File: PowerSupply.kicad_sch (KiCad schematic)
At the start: 44 parts, among them J1 Barrel_Jack, J2 PowerHeader, M1 MouseBites, M2 MouseBites, M3 MouseBites, M4 MouseBites, SW1 SW_SPST, U1 LM7805_TO220, U2 LM7812_TO220, U3 LM7912_TO220

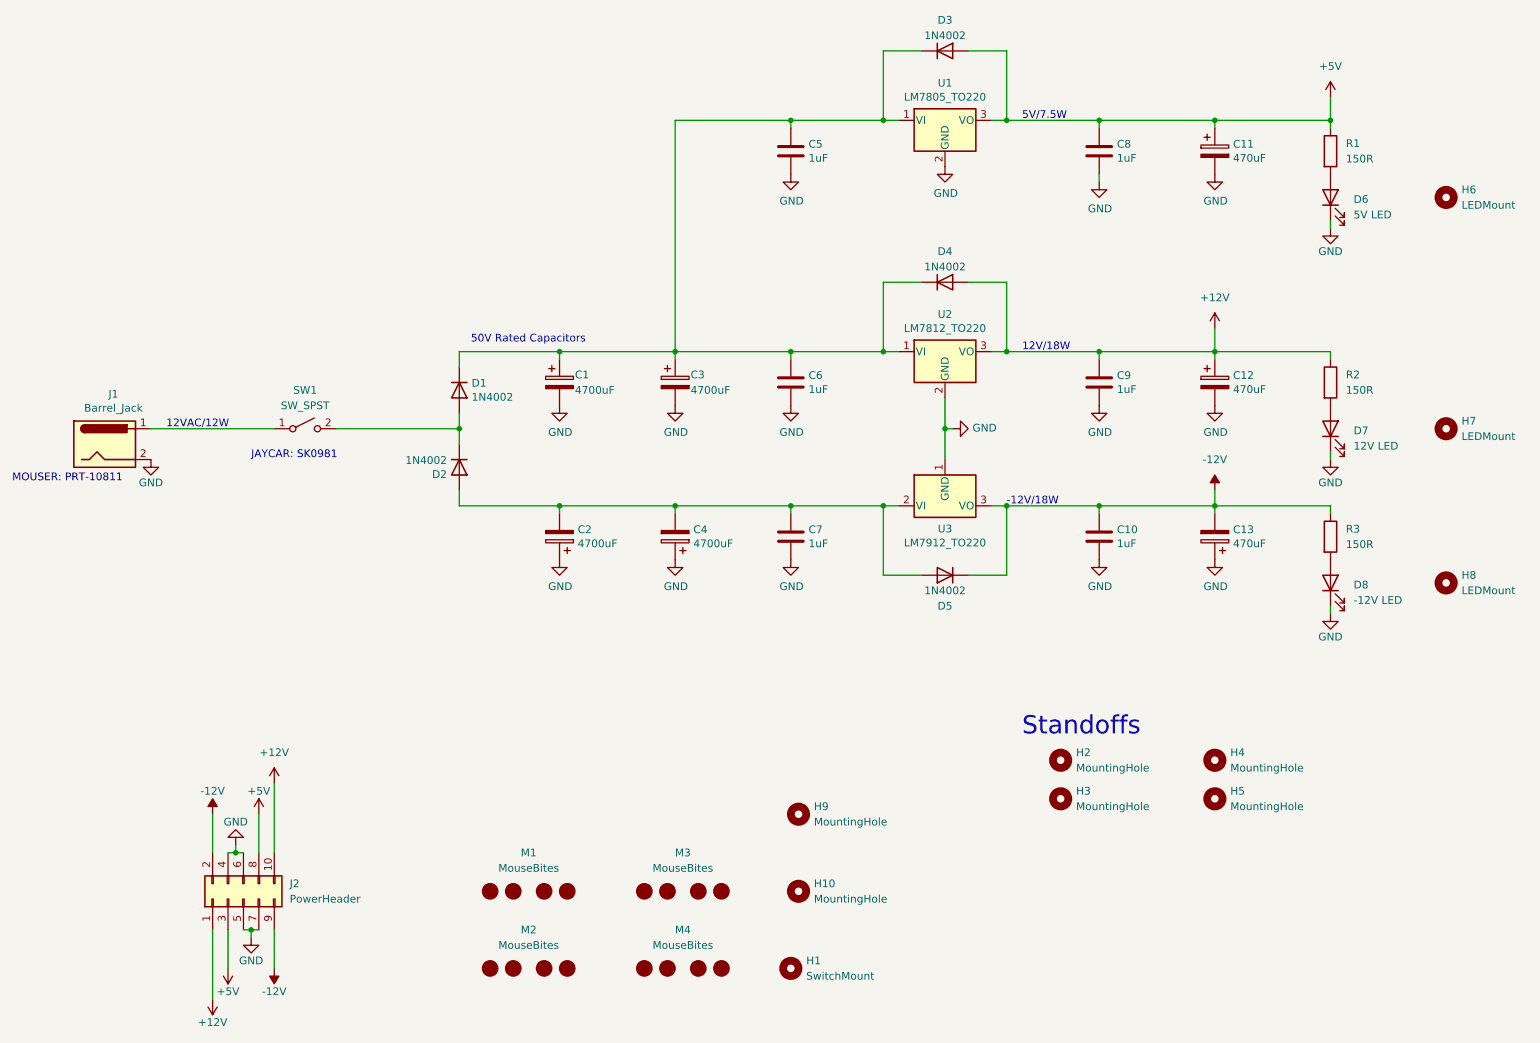
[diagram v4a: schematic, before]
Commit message: Preliminary design on rework
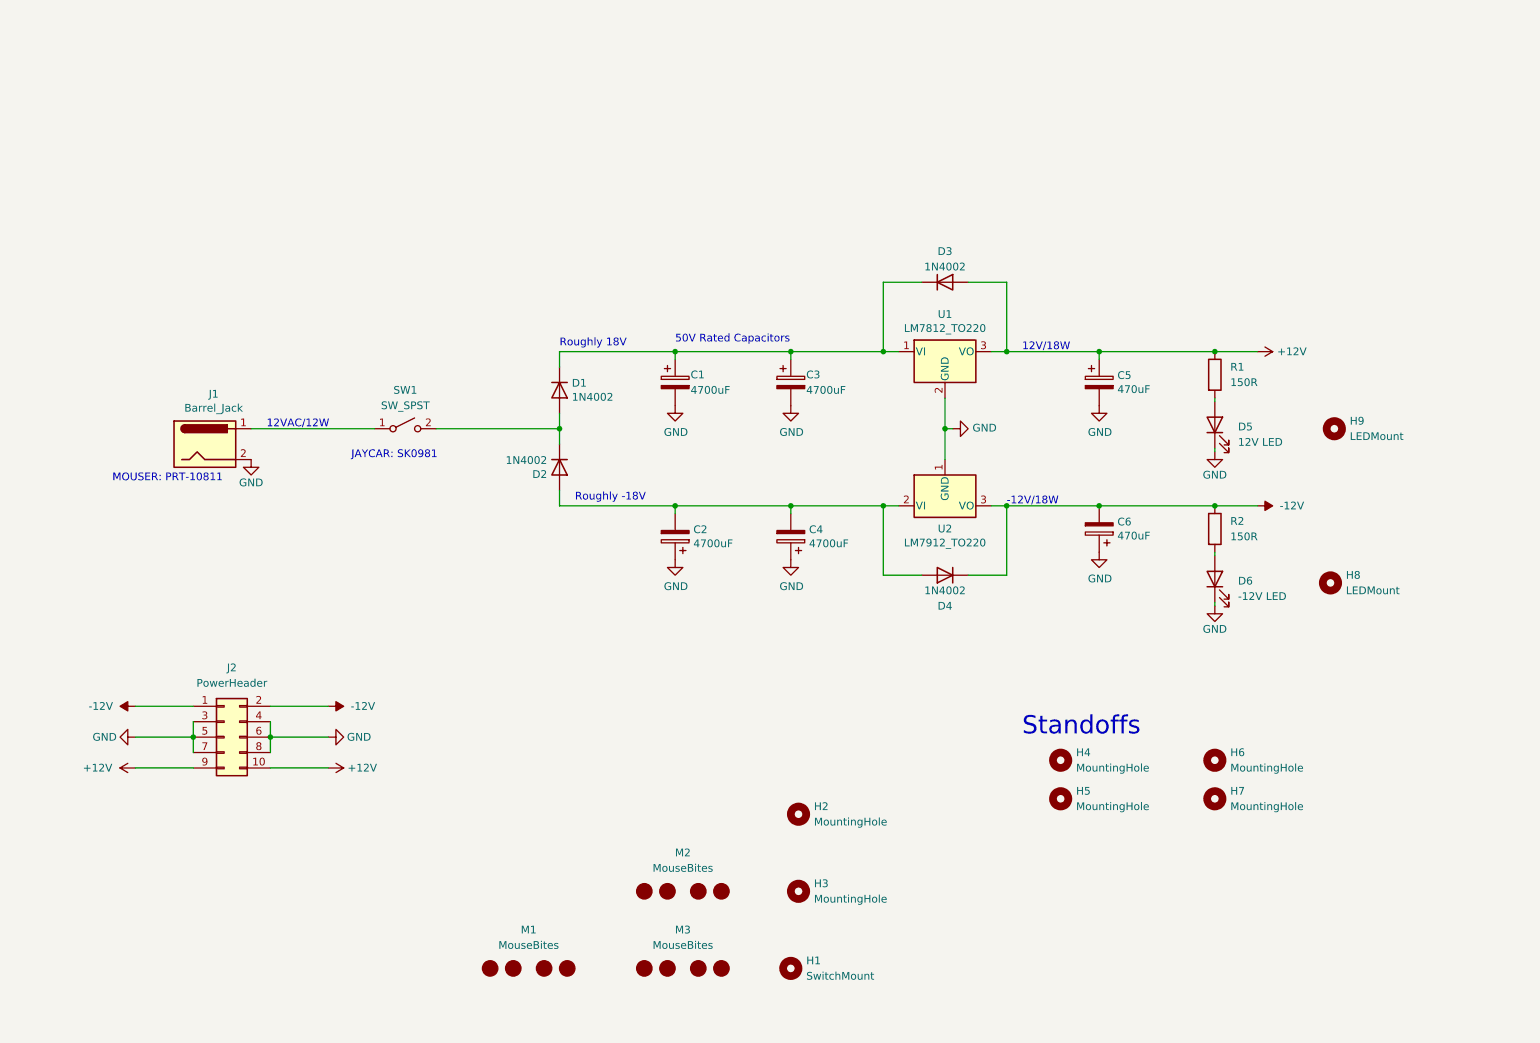
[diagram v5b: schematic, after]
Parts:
- removed C10, C5, C6, C7, C8, C9: 1uF, Capacitor_SMD:C_0805_2012Metric_Pad1.18x1.45mm_HandSolder, symbol Device:C
- removed C11: 470uF, Capacitor_THT:CP_Radial_D10.0mm_P5.00mm, symbol Device:CP
- removed D3: 1N4002, Diode_THT:D_DO-15_P12.70mm_Horizontal, symbol Device:D
- removed D6: 5V LED, LED_THT:LED_D5.0mm, symbol Device:LED
- removed H6: LEDMount, MountingHole:MountingHole_5mm, symbol Mechanical:MountingHole
- removed M1: MouseBites, Panelization:mouse-bite-5mm-slot, symbol Synth:MouseBites
- removed R1: 150R, Resistor_SMD:R_0805_2012Metric_Pad1.20x1.40mm_HandSolder, symbol Device:R
- removed U1: LM7805_TO220, Package_TO_SOT_THT:TO-220-3_Vertical, symbol Regulator_Linear:LM7805_TO220
- D1, D2: footprint Diode_THT:D_DO-15_P12.70mm_Horizontal -> Diode_THT:D_T-1_P5.08mm_Horizontal
- D3: renamed from D4; footprint Diode_THT:D_DO-15_P12.70mm_Horizontal -> Diode_THT:D_T-1_P5.08mm_Horizontal
- D4: renamed from D5; footprint Diode_THT:D_DO-15_P12.70mm_Horizontal -> Diode_THT:D_T-1_P5.08mm_Horizontal
- SW1: footprint Connector_Wire:SolderWire-1sqmm_1x02_P5.4mm_D1.4mm_OD2.7mm_Relief -> Connector_Wire:SolderWire-1.5sqmm_1x02_P6mm_D1.7mm_OD3mm
- renumbered C12 to C5, C13 to C6, D7 to D5, D8 to D6, H9 to H2, H10 to H3, H2 to H4, H3 to H5, H4 to H6, H5 to H7, H7 to H9, M2 to M1, M3 to M2, M4 to M3, R2 to R1, R3 to R2, U2 to U1, U3 to U2
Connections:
- net +5V is gone; now on net GND: J2.3 (Pin_3), J2.8 (Pin_8)
- net +12V: now also J2.9 (Pin_9); no longer J2.1 (Pin_1)
- net -12V: now also J2.1 (Pin_1); no longer J2.9 (Pin_9)
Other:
- note added: "Roughly -18V"
- note added: "Roughly 18V"
- note removed: "5V/7.5W"
- moved on the sheet: C1, C2, C3, C4, C5, C6, D1, D2, D5, D6, H8, H9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

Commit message: Production v2
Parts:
- added C5, C6, C7, C8: 0.1uF, Capacitor_SMD_Handsoldering_AKL:C_0805_2012Metric_Pad1.18x1.45mm, symbol Device:C
- added D7, D8: 1N4002, Diode_THT:D_T-1_P5.08mm_Horizontal, symbol Device:D
- added R1, R2: 1R 1W, Resistor_THT_AKL:R_Axial_DIN0414_L11.9mm_D4.5mm_P15.24mm_Horizontal, symbol Device:R
- R3: renamed from R1; footprint Resistor_SMD:R_0805_2012Metric_Pad1.20x1.40mm_HandSolder -> Resistor_SMD_AKL:R_0805_2012Metric_Pad1.20x1.40mm
- R4: renamed from R2; footprint Resistor_SMD:R_0805_2012Metric_Pad1.20x1.40mm_HandSolder -> Resistor_SMD_AKL:R_0805_2012Metric_Pad1.20x1.40mm
- U1, U2: footprint Package_TO_SOT_THT:TO-220-3_Vertical -> Package_TO_SOT_THT_AKL:TO-220-3_Vertical
- renumbered C6 to C10, C5 to C9, H9 to H6, H8 to H7, H6 to H8, H7 to H9
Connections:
- net +12V: now also C7.1, D7.1 (K)
- net -12V: now also C8.2, D8.2 (A)
- net GND: now also C5.2, C6.1, C7.2, C8.1, D7.2 (A), D8.1 (K)
- net at C3.1, D3.1 (K), U1.1 (VI): now also C5.1, R1.2; no longer C1.1, D1.1 (K)
- net at C4.2, D4.2 (A), U2.2 (VI): now also C6.2, R2.2; no longer C2.2, D2.2 (A)
- new net: C1.1, D1.1 (K), R1.1
- new net: C2.2, D2.2 (A), R2.1
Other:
- note removed: "-12V/18W"
- note removed: "12V/18W"
- note removed: "Roughly -18V"
- note removed: "Roughly 18V"
- moved on the sheet: C1, C10, C2, C3, C4, C9, D1, D2, D3, D4, D5, D6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
